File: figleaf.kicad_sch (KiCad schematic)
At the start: 31 parts, among them U1 Nice_Nano_V2_GRAZ

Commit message: Add power components v1
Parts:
- added H1, H2, H3, H4: M1.6_mounting, Graz_Footprints:m1.6, symbol ScottoKeebs:Placeholder_Mounting_Hole
- added L_J1: Conn_01x02_Socket, Connector_JST:JST_SH_SM02B-SRSS-TB_1x02-1MP_P1.00mm_Horizontal, symbol Connector:Conn_01x02_Socket
- added L_RSW1: SW_RST, Button_Switch_SMD:SW_Tactile_SPST_NO_Straight_CK_PTS636Sx25SMTRLFS, symbol Lily58_Pro-rescue:SW_RST-Lily58-cache
- added L_SW1: SW_SPDT, Button_Switch_SMD:SW_SPDT_PCM12, symbol Switch:SW_SPDT
- U1: footprint MCU:Nice_Nano_V2 -> Graz_Footprints:Nice_Nano_V2_Graz
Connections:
- net GND_L: now also L_J1.2 (Pin_2), L_RSW1.1
- net RAW_L: now also L_SW1.3 (C)
- net RESET_L: now also L_RSW1.2
- new net +BATT_L: L_J1.1 (Pin_1), L_SW1.2 (B)
- no-connect marks 11 -> 23

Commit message: progress PCB
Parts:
- S1, S10, S11, S12, S13, S14, S15, S16, S17, S18, S19, S2, S20, S21, S22, S23, S24, S25, S26, S27, S28, S29, S3, S30, S4, S5, S6, S7, S8, S9: footprint Graz_Footprints:One Key Module -> Graz_Footprints:One Key Module Graz
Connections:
- net +BATT_L: now also L_J1.2 (Pin_2); no longer L_J1.1 (Pin_1)
- net GND_L: now also L_J1.1 (Pin_1); no longer L_J1.2 (Pin_2)
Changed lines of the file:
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@@
 	(wire
 		(pts
-			(xy 295.91 215.9) (xy 297.18 215.9)
-		)
-		(stroke
-			(width 0)
-			(type default)
-		)
-	)
-	(wire
-		(pts
 			(xy 63.5 213.36) (xy 63.5 218.44)
 		)
@@
 	(wire
 		(pts
-			(xy 295.91 213.36) (xy 297.18 213.36)
-		)
-		(stroke
-			(width 0)
-			(type default)
-		)
-	)
-	(wire
-		(pts
 			(xy 99.06 177.8) (xy 104.14 177.8)
 		)
@@
 			)
 		)
-		(property "Footprint" "Graz_Footprints:One Key Module"
+		(property "Footprint" "Graz_Footprints:One Key Module Graz"
 			(at 39.37 174.0235 0)
 			(effects
@@
 			)
 		)
-		(property "Footprint" "Graz_Footprints:One Key Module"
+		(property "Footprint" "Graz_Footprints:One Key Module Graz"
 			(at 83.82 147.32 0)
 			(effects
@@
 			)
 		)
-		(property "Footprint" "Graz_Footprints:One Key Module"
+		(property "Footprint" "Graz_Footprints:One Key Module Graz"
 			(at 134.62 147.32 0)
 			(effects
@@
 			)
 		)
-		(property "Footprint" "Graz_Footprints:One Key Module"
+		(property "Footprint" "Graz_Footprints:One Key Module Graz"
 			(at 134.62 198.12 0)
 			(effects
@@
 			)
 		)
-		(property "Footprint" "Graz_Footprints:One Key Module"
+		(property "Footprint" "Graz_Footprints:One Key Module Graz"
 			(at 39.37 148.6235 0)
 			(effects
@@
 			)
 		)
-		(property "Footprint" "Graz_Footprints:One Key Module"
+		(property "Footprint" "Graz_Footprints:One Key Module Graz"
 			(at 109.22 147.32 0)
 			(effects
@@
 	(symbol
 		(lib_id "power:+BATT")
-		(at 295.91 213.36 90)
+		(at 297.18 215.9 90)
 		(unit 1)
 		(exclude_from_sim no)
@@
 		(on_board yes)
 		(dnp no)
-		(fields_autoplaced yes)
 		(property "Reference" "#PWR015"
-			(at 299.72 213.36 0)
+			(at 300.99 215.9 0)
 			(effects
 				(font
@@
 		)
 		(property "Value" "+BATT_L"
-			(at 292.1 213.3599 90)
+			(at 293.37 215.8999 90)
 			(effects
 				(font
@@
 		)
 		(property "Footprint" ""
-			(at 295.91 213.36 0)
+			(at 297.18 215.9 0)
 			(effects
 				(font
@@
 		)
 		(property "Datasheet" ""
-			(at 295.91 213.36 0)
+			(at 297.18 215.9 0)
 			(effects
 				(font
@@
 		)
 		(property "Description" "Power symbol creates a global label with name \"+BATT\""
-			(at 295.91 213.36 0)
+			(at 297.18 215.9 0)
 			(effects
 				(font
@@
 			)
 		)
-		(property "Footprint" "Graz_Footprints:One Key Module"
+		(property "Footprint" "Graz_Footprints:One Key Module Graz"
 			(at 109.22 198.12 0)
 			(effects
@@
 			)
 		)
-		(property "Footprint" "Graz_Footprints:One Key Module"
+		(property "Footprint" "Graz_Footprints:One Key Module Graz"
 			(at 160.02 198.12 0)
 			(effects
@@
 			)
 		)
-		(property "Footprint" "Graz_Footprints:One Key Module"
+		(property "Footprint" "Graz_Footprints:One Key Module Graz"
 			(at 109.22 172.72 0)
 			(effects
@@
 			)
 		)
-		(property "Footprint" "Graz_Footprints:One Key Module"
+		(property "Footprint" "Graz_Footprints:One Key Module Graz"
 			(at 160.02 121.92 0)
 			(effects
@@
 			)
 		)
-		(property "Footprint" "Graz_Footprints:One Key Module"
+		(property "Footprint" "Graz_Footprints:One Key Module Graz"
 			(at 83.82 121.92 0)
 			(effects
@@
 			)
 		)
-		(property "Footprint" "Graz_Footprints:One Key Module"
+		(property "Footprint" "Graz_Footprints:One Key Module Graz"
 			(at 39.37 123.2235 0)
 			(effects
@@
 			)
 		)
-		(property "Footprint" "Graz_Footprints:One Key Module"
+		(property "Footprint" "Graz_Footprints:One Key Module Graz"
 			(at 83.82 223.52 0)
 			(effects
@@
 			)
 		)
-		(property "Footprint" "Graz_Footprints:One Key Module"
+		(property "Footprint" "Graz_Footprints:One Key Module Graz"
 			(at 160.02 147.32 0)
 			(effects
@@
 			)
 		)
-		(property "Footprint" "Graz_Footprints:One Key Module"
+		(property "Footprint" "Graz_Footprints:One Key Module Graz"
 			(at 160.02 223.52 0)
 			(effects
@@
 			)
 		)
-		(property "Footprint" "Graz_Footprints:One Key Module"
+		(property "Footprint" "Graz_Footprints:One Key Module Graz"
 			(at 185.42 198.12 0)
 			(effects
@@
 			)
 		)
-		(property "Footprint" "Graz_Footprints:One Key Module"
+		(property "Footprint" "Graz_Footprints:One Key Module Graz"
 			(at 185.42 147.32 0)
 			(effects
@@
 			)
 		)
-		(property "Footprint" "Graz_Footprints:One Key Module"
+		(property "Footprint" "Graz_Footprints:One Key Module Graz"
 			(at 83.82 172.72 0)
 			(effects
@@
 			)
 		)
-		(property "Footprint" "Graz_Footprints:One Key Module"
+		(property "Footprint" "Graz_Footprints:One Key Module Graz"
 			(at 39.37 199.4235 0)
 			(effects
@@
 			)
 		)
-		(property "Footprint" "Graz_Footprints:One Key Module"
+		(property "Footprint" "Graz_Footprints:One Key Module Graz"
 			(at 109.22 121.92 0)
 			(effects
@@
 			)
 		)
-		(property "Footprint" "Graz_Footprints:One Key Module"
+		(property "Footprint" "Graz_Footprints:One Key Module Graz"
 			(at 160.02 172.72 0)
 			(effects
@@
 			)
 		)
-		(property "Footprint" "Graz_Footprints:One Key Module"
+		(property "Footprint" "Graz_Footprints:One Key Module Graz"
 			(at 39.37 224.8235 0)
 			(effects
@@
 			)
 		)
-		(property "Footprint" "Graz_Footprints:One Key Module"
+		(property "Footprint" "Graz_Footprints:One Key Module Graz"
 			(at 83.82 198.12 0)
 			(effects
@@
 	(symbol
 		(lib_id "power:GND")
-		(at 295.91 215.9 0)
+		(at 297.18 213.36 270)
 		(unit 1)
 		(exclude_from_sim no)
@@
 		(fields_autoplaced yes)
 		(property "Reference" "#PWR016"
-			(at 295.91 222.25 0)
+			(at 290.83 213.36 0)
 			(effects
 				(font
@@
 		)
 		(property "Value" "GND_L"
-			(at 295.91 220.98 0)
+			(at 293.37 213.3599 90)
 			(effects
 				(font
 					(size 1.27 1.27)
 				)
+				(justify right)
 			)
 		)
 		(property "Footprint" ""
-			(at 295.91 215.9 0)
+			(at 297.18 213.36 0)
 			(effects
 				(font
@@
 		)
 		(property "Datasheet" ""
-			(at 295.91 215.9 0)
+			(at 297.18 213.36 0)
 			(effects
 				(font
@@
 		)
 		(property "Description" "Power symbol creates a global label with name \"GND\" , ground"
-			(at 295.91 215.9 0)
+			(at 297.18 213.36 0)
 			(effects
 				(font
@@
 			)
 		)
-		(property "Footprint" "Graz_Footprints:One Key Module"
+		(property "Footprint" "Graz_Footprints:One Key Module Graz"
 			(at 134.62 172.72 0)
 			(effects
@@
 			)
 		)
-		(property "Footprint" "Graz_Footprints:One Key Module"
+		(property "Footprint" "Graz_Footprints:One Key Module Graz"
 			(at 185.42 172.72 0)
 			(effects
@@
 			)
 		)
-		(property "Footprint" "Graz_Footprints:One Key Module"
+		(property "Footprint" "Graz_Footprints:One Key Module Graz"
 			(at 109.22 223.52 0)
 			(effects
@@
 			)
 		)
-		(property "Footprint" "Graz_Footprints:One Key Module"
+		(property "Footprint" "Graz_Footprints:One Key Module Graz"
 			(at 134.62 121.92 0)
 			(effects
@@
 			)
 		)
-		(property "Footprint" "Graz_Footprints:One Key Module"
+		(property "Footprint" "Graz_Footprints:One Key Module Graz"
 			(at 134.62 223.52 0)
 			(effects
@@
 			)
 		)
-		(property "Footprint" "Graz_Footprints:One Key Module"
+		(property "Footprint" "Graz_Footprints:One Key Module Graz"
 			(at 185.42 223.52 0)
 			(effects
@@
 			)
 		)
-		(property "Footprint" "Graz_Footprints:One Key Module"
+		(property "Footprint" "Graz_Footprints:One Key Module Graz"
 			(at 185.42 121.92 0)
 			(effects

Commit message: Add sidemounted reset
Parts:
- L_RSW1: footprint Button_Switch_SMD:SW_Tactile_SPST_NO_Straight_CK_PTS636Sx25SMTRLFS -> Button_Switch_SMD:SW_SPST_B3U-3000P-B
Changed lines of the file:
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@@
 			)
 		)
-		(property "Footprint" "Button_Switch_SMD:SW_Tactile_SPST_NO_Straight_CK_PTS636Sx25SMTRLFS"
+		(property "Footprint" "Button_Switch_SMD:SW_SPST_B3U-3000P-B"
 			(at 264.16 217.17 0)
 			(effects

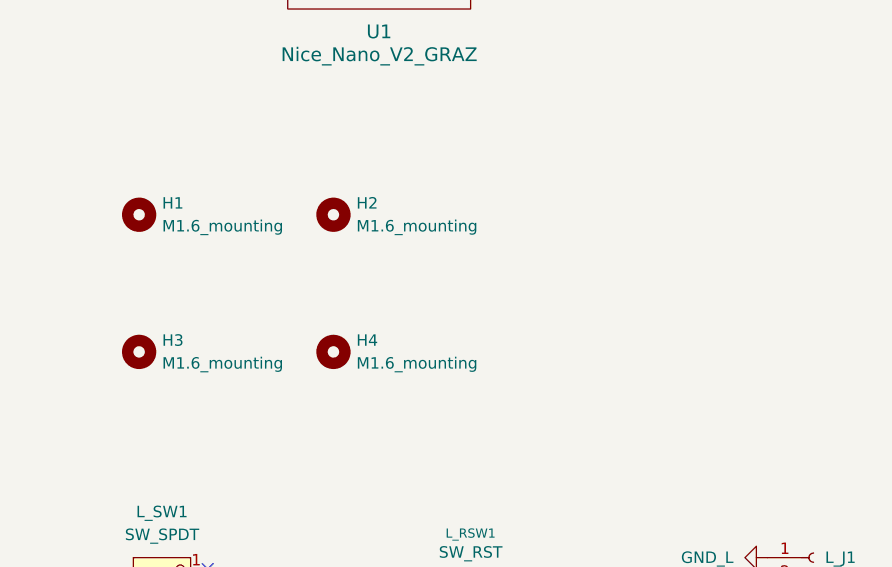
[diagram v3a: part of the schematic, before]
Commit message: add more mounting holes
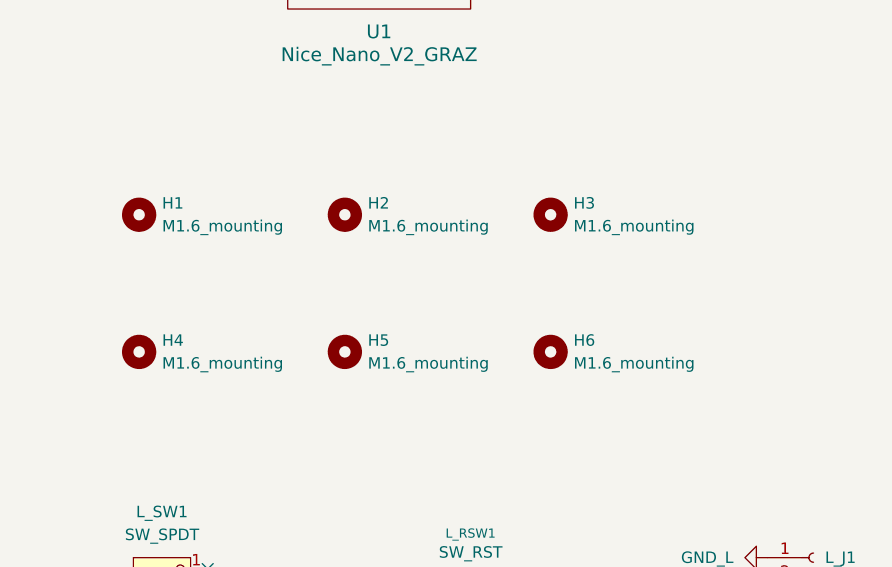
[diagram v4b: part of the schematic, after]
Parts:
- added H5, H6: M1.6_mounting, Graz_Footprints:m1.6, symbol ScottoKeebs:Placeholder_Mounting_Hole
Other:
- moved on the sheet: H2, H3, H4
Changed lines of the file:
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@@
 	)
 	(symbol
+		(lib_id "ScottoKeebs:Placeholder_Mounting_Hole")
+		(at 273.05 190.5 0)
+		(unit 1)
+		(exclude_from_sim no)
+		(in_bom yes)
+		(on_board yes)
+		(dnp no)
+		(fields_autoplaced yes)
+		(property "Reference" "H6"
+			(at 275.59 189.2299 0)
+			(effects
+				(font
+					(size 1.27 1.27)
+				)
+				(justify left)
+			)
+		)
+		(property "Value" "M1.6_mounting"
+			(at 275.59 191.7699 0)
+			(effects
+				(font
+					(size 1.27 1.27)
+				)
+				(justify left)
+			)
+		)
+		(property "Footprint" "Graz_Footprints:m1.6"
+			(at 273.05 190.5 0)
+			(effects
+				(font
+					(size 1.27 1.27)
+				)
+				(hide yes)
+			)
+		)
+		(property "Datasheet" "~"
+			(at 273.05 190.5 0)
+			(effects
+				(font
+					(size 1.27 1.27)
+				)
+				(hide yes)
+			)
+		)
+		(property "Description" "Mounting Hole without connection"
+			(at 273.05 190.5 0)
+			(effects
+				(font
+					(size 1.27 1.27)
+				)
+				(hide yes)
+			)
+		)
+		(instances
+			(project "figleaf"
+				(path "/fd9c0cf8-91e7-46bd-8f73-27ef3bc34e44"
+					(reference "H6")
+					(unit 1)
+				)
+			)
+		)
+	)
+	(symbol
 		(lib_id "0_graz_symbols:SW_OKM")
 		(at 88.9 152.4 0)
@@
 	)
 	(symbol
+		(lib_id "ScottoKeebs:Placeholder_Mounting_Hole")
+		(at 250.19 190.5 0)
+		(unit 1)
+		(exclude_from_sim no)
+		(in_bom yes)
+		(on_board yes)
+		(dnp no)
+		(fields_autoplaced yes)
+		(property "Reference" "H5"
+			(at 252.73 189.2299 0)
+			(effects
+				(font
+					(size 1.27 1.27)
+				)
+				(justify left)
+			)
+		)
+		(property "Value" "M1.6_mounting"
+			(at 252.73 191.7699 0)
+			(effects
+				(font
+					(size 1.27 1.27)
+				)
+				(justify left)
+			)
+		)
+		(property "Footprint" "Graz_Footprints:m1.6"
+			(at 250.19 190.5 0)
+			(effects
+				(font
+					(size 1.27 1.27)
+				)
+				(hide yes)
+			)
+		)
+		(property "Datasheet" "~"
+			(at 250.19 190.5 0)
+			(effects
+				(font
+					(size 1.27 1.27)
+				)
+				(hide yes)
+			)
+		)
+		(property "Description" "Mounting Hole without connection"
+			(at 250.19 190.5 0)
+			(effects
+				(font
+					(size 1.27 1.27)
+				)
+				(hide yes)
+			)
+		)
+		(instances
+			(project "figleaf"
+				(path "/fd9c0cf8-91e7-46bd-8f73-27ef3bc34e44"
+					(reference "H5")
+					(unit 1)
+				)
+			)
+		)
+	)
+	(symbol
 		(lib_id "power:GND")
 		(at 195.58 238.76 0)
@@
 	(symbol
 		(lib_id "ScottoKeebs:Placeholder_Mounting_Hole")
-		(at 227.33 190.5 0)
+		(at 273.05 175.26 0)
 		(unit 1)
 		(exclude_from_sim no)
@@
 		(fields_autoplaced yes)
 		(property "Reference" "H3"
-			(at 229.87 189.2299 0)
+			(at 275.59 173.9899 0)
 			(effects
 				(font
@@
 		)
 		(property "Value" "M1.6_mounting"
-			(at 229.87 191.7699 0)
+			(at 275.59 176.5299 0)
 			(effects
 				(font
@@
 		)
 		(property "Footprint" "Graz_Footprints:m1.6"
-			(at 227.33 190.5 0)
+			(at 273.05 175.26 0)
 			(effects
 				(font
@@
 		)
 		(property "Datasheet" "~"
-			(at 227.33 190.5 0)
+			(at 273.05 175.26 0)
 			(effects
 				(font
@@
 		)
 		(property "Description" "Mounting Hole without connection"
-			(at 227.33 190.5 0)
+			(at 273.05 175.26 0)
 			(effects
 				(font
@@
 	(symbol
 		(lib_id "ScottoKeebs:Placeholder_Mounting_Hole")
-		(at 248.92 175.26 0)
+		(at 250.19 175.26 0)
 		(unit 1)
 		(exclude_from_sim no)
@@
 		(fields_autoplaced yes)
 		(property "Reference" "H2"
-			(at 251.46 173.9899 0)
+			(at 252.73 173.9899 0)
 			(effects
 				(font
@@
 		)
 		(property "Value" "M1.6_mounting"
-			(at 251.46 176.5299 0)
+			(at 252.73 176.5299 0)
 			(effects
 				(font
@@
 		)
 		(property "Footprint" "Graz_Footprints:m1.6"
-			(at 248.92 175.26 0)
+			(at 250.19 175.26 0)
 			(effects
 				(font
@@
 		)
 		(property "Datasheet" "~"
-			(at 248.92 175.26 0)
+			(at 250.19 175.26 0)
 			(effects
 				(font
@@
 		)
 		(property "Description" "Mounting Hole without connection"
-			(at 248.92 175.26 0)
+			(at 250.19 175.26 0)
 			(effects
 				(font
@@
 	(symbol
 		(lib_id "ScottoKeebs:Placeholder_Mounting_Hole")
-		(at 248.92 190.5 0)
+		(at 227.33 190.5 0)
 		(unit 1)
 		(exclude_from_sim no)
@@
 		(fields_autoplaced yes)
 		(property "Reference" "H4"
-			(at 251.46 189.2299 0)
+			(at 229.87 189.2299 0)
 			(effects
 				(font
@@
 		)
 		(property "Value" "M1.6_mounting"
-			(at 251.46 191.7699 0)
+			(at 229.87 191.7699 0)
 			(effects
 				(font
@@
 		)
 		(property "Footprint" "Graz_Footprints:m1.6"
-			(at 248.92 190.5 0)
+			(at 227.33 190.5 0)
 			(effects
 				(font
@@
 		)
 		(property "Datasheet" "~"
-			(at 248.92 190.5 0)
+			(at 227.33 190.5 0)
 			(effects
 				(font
@@
 		)
 		(property "Description" "Mounting Hole without connection"
-			(at 248.92 190.5 0)
+			(at 227.33 190.5 0)
 			(effects
 				(font

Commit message: start with seeed mcu
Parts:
- added U2: XIAO-nRF52840-Plus-SMD, Graz_Footprints:XIAO-nRF52840-Plus-SMD, symbol 0_graz_symbols:XIAO-nRF52840_Plus_SMD
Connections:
- net GND_L: now also U2.13 (GND), U2.27 (GND), U2.33 (GND)
- net RAW_L: now also U2.32 (VBAT)
- net RESET_L: now also U2.26 (REST)
- net col_0: now also U2.10 (P1.14_D9_MISO)
- net col_1: now also U2.9 (P1.13_D8_SCK)
- net col_2: now also U2.8 (P1.12_D7_RX)
- net col_3: now also U2.21 (P1.03_D17_SCK1)
- net col_4: now also U2.22 (P1.05_D18_MISO1)
- net col_5: now also U2.23 (P1.07_D19_MOSI1)
- net row_0: now also U2.1 (P0.02_A0_D0)
- net row_1: now also U2.2 (P0.03_A1_D1)
- net row_2: now also U2.3 (P0.28_A2_D2)
- net row_3: now also U2.4 (P0.29_A3_D3)
- net row_4: now also U2.5 (P0.04_A4_D4_SDA)
- no-connect marks 23 -> 26
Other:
- moved on the sheet: L_J1, L_RSW1, L_SW1, U1
